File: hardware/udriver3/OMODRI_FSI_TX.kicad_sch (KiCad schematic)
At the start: 7 parts, among them J10 Conn_01x07, U13 TPD6E05U06, U14 DSLVDS1047

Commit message: Almost done, Rework power plane, change FSI DF13 (possibly wrong footprint (see pin 1), add 3d for all components, connect VM and 12V0, ...
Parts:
- J10: footprint udriver3:Hirose_DF13-07P-1.25DSA_1x07_P1.25mm_Vertical -> udriver3:DF137P125H75
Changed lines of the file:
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@@
       (effects (font (size 1.27 1.27)) (justify left))
     )
-    (property "Footprint" "udriver3:Hirose_DF13-07P-1.25DSA_1x07_P1.25mm_Vertical" (id 2) (at 241.935 80.645 0)
+    (property "Footprint" "udriver3:DF137P125H75" (id 2) (at 241.935 80.645 0)
       (effects (font (size 1.27 1.27)) hide)
     )

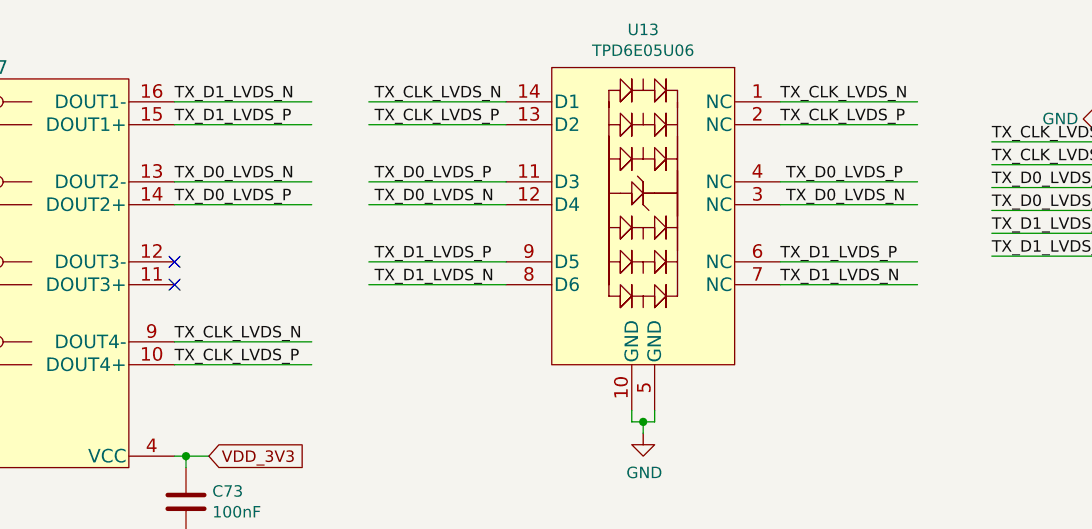
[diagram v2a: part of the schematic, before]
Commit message: Schematics update. 12V0 and 5V0 power supplies not finished yet. RS485 added but not connected to F28388 mcu.
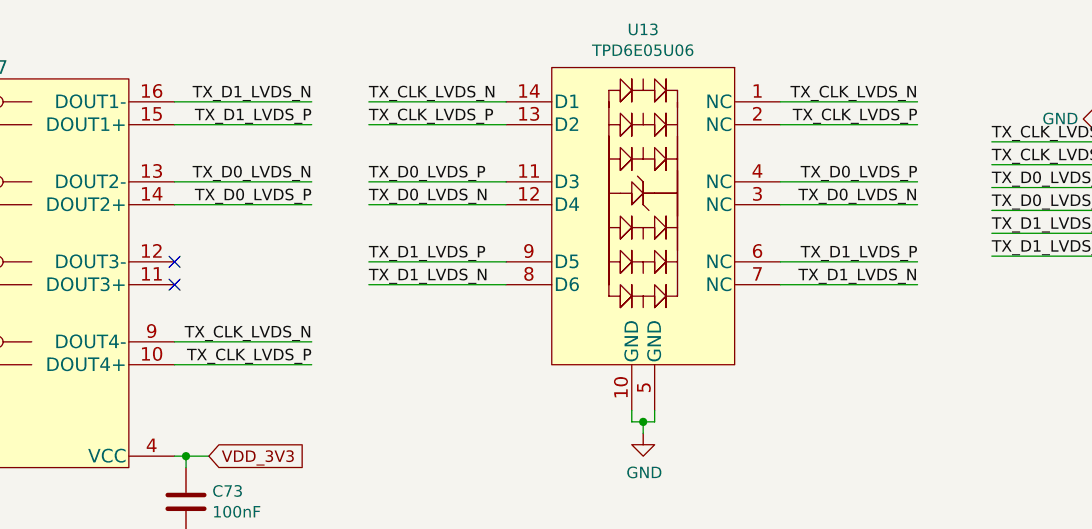
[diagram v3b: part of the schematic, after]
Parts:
- C73: Rated Voltage 10V -> 25V
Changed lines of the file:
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@@
     (title "Open MOtor DRiver Initiative (OMODRI)")
     (date "2020-12-16")
-    (rev "1.1")
+    (rev "2.0")
     (company "LAAS/CNRS")
   )
@@
     (stroke (width 0) (type default) (color 0 0 0 0))
   )
-  (label "TX_D0_LVDS_P" (at 153.035 80.01 0)
+  (label "TX_D0_LVDS_P" (at 152.4 80.01 0)
     (effects (font (size 1.27 1.27)) (justify left bottom))
   )
@@
     (effects (font (size 1.27 1.27)) (justify left bottom))
   )
-  (label "TX_CLK_LVDS_N" (at 153.035 71.12 0)
-    (effects (font (size 1.27 1.27)) (justify left bottom))
-  )
-  (label "TX_D0_LVDS_N" (at 198.755 82.55 0)
-    (effects (font (size 1.27 1.27)) (justify left bottom))
-  )
-  (label "TX_CLK_LVDS_P" (at 153.035 73.66 0)
-    (effects (font (size 1.27 1.27)) (justify left bottom))
-  )
-  (label "TX_CLK_LVDS_P" (at 198.12 73.66 0)
-    (effects (font (size 1.27 1.27)) (justify left bottom))
-  )
-  (label "TX_D1_LVDS_P" (at 130.81 73.66 0)
-    (effects (font (size 1.27 1.27)) (justify left bottom))
-  )
-  (label "TX_D1_LVDS_N" (at 130.81 71.12 0)
-    (effects (font (size 1.27 1.27)) (justify left bottom))
-  )
-  (label "TX_D0_LVDS_N" (at 153.035 82.55 0)
-    (effects (font (size 1.27 1.27)) (justify left bottom))
-  )
-  (label "TX_D0_LVDS_P" (at 198.755 80.01 0)
-    (effects (font (size 1.27 1.27)) (justify left bottom))
+  (label "TX_CLK_LVDS_N" (at 152.4 71.12 0)
+    (effects (font (size 1.27 1.27)) (justify left bottom))
+  )
+  (label "TX_D0_LVDS_N" (at 213.36 82.55 180)
+    (effects (font (size 1.27 1.27)) (justify right bottom))
+  )
+  (label "TX_CLK_LVDS_P" (at 152.4 73.66 0)
+    (effects (font (size 1.27 1.27)) (justify left bottom))
+  )
+  (label "TX_CLK_LVDS_P" (at 213.36 73.66 180)
+    (effects (font (size 1.27 1.27)) (justify right bottom))
+  )
+  (label "TX_D1_LVDS_P" (at 146.05 73.66 180)
+    (effects (font (size 1.27 1.27)) (justify right bottom))
+  )
+  (label "TX_D1_LVDS_N" (at 146.05 71.12 180)
+    (effects (font (size 1.27 1.27)) (justify right bottom))
+  )
+  (label "TX_D0_LVDS_N" (at 152.4 82.55 0)
+    (effects (font (size 1.27 1.27)) (justify left bottom))
+  )
+  (label "TX_D0_LVDS_P" (at 213.36 80.01 180)
+    (effects (font (size 1.27 1.27)) (justify right bottom))
   )
   (label "TX_D1_LVDS_N" (at 221.615 88.265 0)
     (effects (font (size 1.27 1.27)) (justify left bottom))
   )
-  (label "TX_D0_LVDS_P" (at 130.81 82.55 0)
-    (effects (font (size 1.27 1.27)) (justify left bottom))
+  (label "TX_D0_LVDS_P" (at 146.05 82.55 180)
+    (effects (font (size 1.27 1.27)) (justify right bottom))
   )
   (label "TX_CLK_LVDS_N" (at 221.615 75.565 0)
     (effects (font (size 1.27 1.27)) (justify left bottom))
   )
-  (label "TX_D1_LVDS_N" (at 153.035 91.44 0)
-    (effects (font (size 1.27 1.27)) (justify left bottom))
-  )
-  (label "TX_D1_LVDS_N" (at 198.12 91.44 0)
-    (effects (font (size 1.27 1.27)) (justify left bottom))
-  )
-  (label "TX_D0_LVDS_N" (at 130.81 80.01 0)
-    (effects (font (size 1.27 1.27)) (justify left bottom))
+  (label "TX_D1_LVDS_N" (at 152.4 91.44 0)
+    (effects (font (size 1.27 1.27)) (justify left bottom))
+  )
+  (label "TX_D1_LVDS_N" (at 213.36 91.44 180)
+    (effects (font (size 1.27 1.27)) (justify right bottom))
+  )
+  (label "TX_D0_LVDS_N" (at 146.05 80.01 180)
+    (effects (font (size 1.27 1.27)) (justify right bottom))
   )
   (label "TX_D0_LVDS_N" (at 221.615 80.645 0)
     (effects (font (size 1.27 1.27)) (justify left bottom))
   )
-  (label "TX_D1_LVDS_P" (at 153.035 88.9 0)
-    (effects (font (size 1.27 1.27)) (justify left bottom))
-  )
-  (label "TX_CLK_LVDS_P" (at 130.81 100.33 0)
-    (effects (font (size 1.27 1.27)) (justify left bottom))
+  (label "TX_D1_LVDS_P" (at 152.4 88.9 0)
+    (effects (font (size 1.27 1.27)) (justify left bottom))
+  )
+  (label "TX_CLK_LVDS_P" (at 146.05 100.33 180)
+    (effects (font (size 1.27 1.27)) (justify right bottom))
   )
   (label "TX_D1_LVDS_P" (at 221.615 85.725 0)
     (effects (font (size 1.27 1.27)) (justify left bottom))
   )
-  (label "TX_CLK_LVDS_N" (at 198.12 71.12 0)
-    (effects (font (size 1.27 1.27)) (justify left bottom))
-  )
-  (label "TX_CLK_LVDS_N" (at 130.81 97.79 0)
-    (effects (font (size 1.27 1.27)) (justify left bottom))
-  )
-  (label "TX_D1_LVDS_P" (at 198.12 88.9 0)
-    (effects (font (size 1.27 1.27)) (justify left bottom))
+  (label "TX_CLK_LVDS_N" (at 213.36 71.12 180)
+    (effects (font (size 1.27 1.27)) (justify right bottom))
+  )
+  (label "TX_CLK_LVDS_N" (at 146.05 97.79 180)
+    (effects (font (size 1.27 1.27)) (justify right bottom))
+  )
+  (label "TX_D1_LVDS_P" (at 213.36 88.9 180)
+    (effects (font (size 1.27 1.27)) (justify right bottom))
   )
   (global_label "VDD_3V3" (shape input) (at 134.62 110.49 0) (fields_autoplaced)
@@
       (effects (font (size 1.27 1.27)) hide)
     )
-    (property "Rated Voltage" "10V" (id 5) (at 132.08 115.57 0)
-      (effects (font (size 1.27 1.27)) hide)
-    )
+    (property "Rated Voltage" "25V" (id 5) (at 132.08 115.57 0)
+      (effects (font (size 1.27 1.27)) hide)
+    )

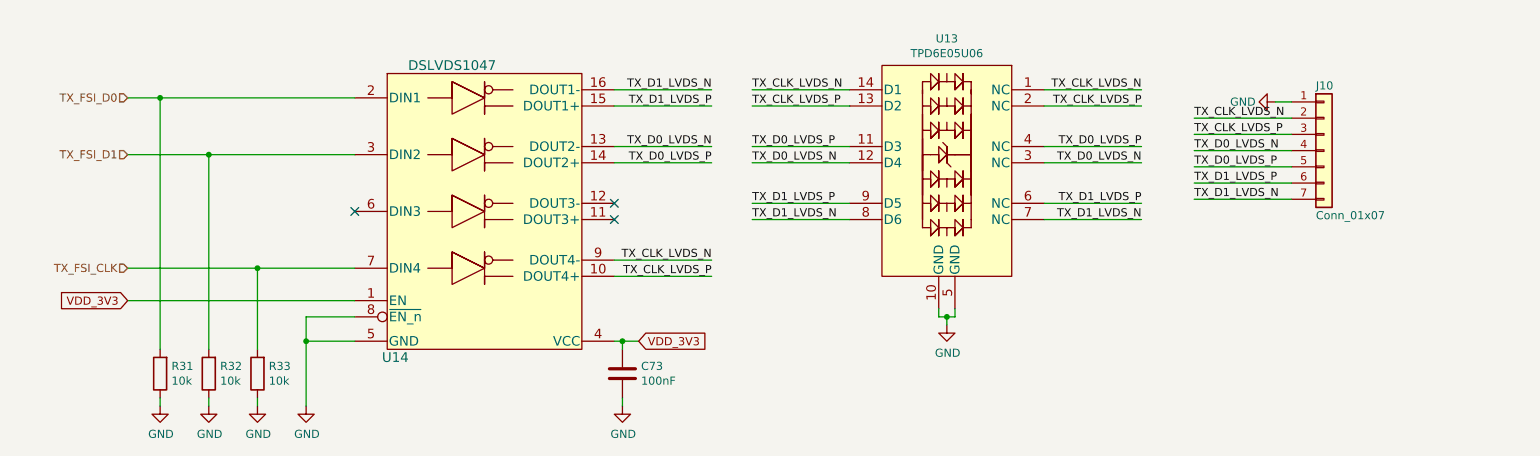
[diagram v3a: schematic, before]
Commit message: Temporary version of udrive3 v2.0. - In schematic there are 2 solutions for DC/DC buck converter. - PCB routing is not finished yet.
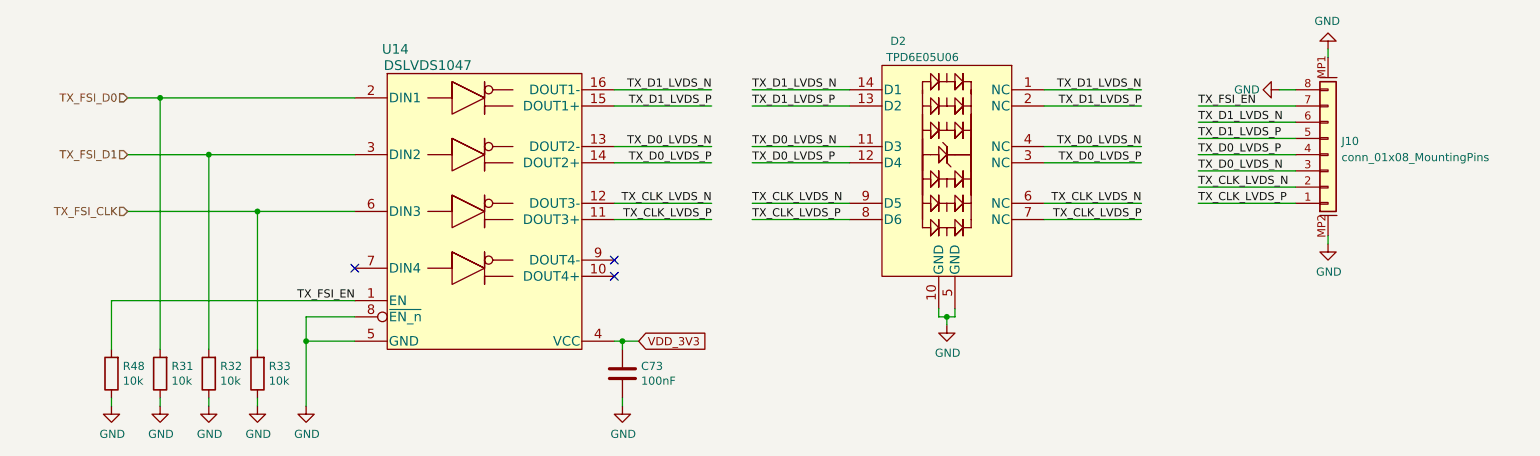
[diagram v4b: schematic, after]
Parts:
- removed J10: Conn_01x07, udriver3:DF137P125H75, symbol Connector_Generic:Conn_01x07
- added J10: conn_01x08_MountingPins, udriver3:Molex_FBH1_1x08-2MP_P0.50mm_Horizontal, symbol omodri_lib:conn_01x08_MountingPins
- added R48: 10k, Resistor_SMD:R_0201_0603Metric, symbol Device:R
- D2: renamed from U13; footprint udriver3:USON_14 -> udrive3:USON_14
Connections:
- net GND: now also J10.8 (Pin_8), J10.MP1 (MountPin1), J10.MP2 (MountPin2), R48.1
- net TX_CLK_LVDS_N: now also D2.6 (NC), D2.9 (D5), U14.12 (DOUT3-), J10.2 (Pin_2); no longer D2.1 (NC), D2.14 (D1), U14.9 (DOUT4-)
- net TX_CLK_LVDS_P: now also D2.7 (NC), D2.8 (D6), U14.11 (DOUT3+), J10.1 (Pin_1); no longer D2.13 (D2), D2.2 (NC), U14.10 (DOUT4+)
- net TX_D0_LVDS_N: now also D2.11 (D3), D2.4 (NC), J10.3 (Pin_3); no longer D2.12 (D4), D2.3 (NC)
- net TX_D0_LVDS_P: now also D2.12 (D4), D2.3 (NC), J10.4 (Pin_4); no longer D2.11 (D3), D2.4 (NC)
- net TX_D1_LVDS_N: now also D2.1 (NC), D2.14 (D1), J10.6 (Pin_6); no longer D2.7 (NC), D2.8 (D6)
- net TX_D1_LVDS_P: now also D2.13 (D2), D2.2 (NC), J10.5 (Pin_5); no longer D2.6 (NC), D2.9 (D5)
- net TX_FSI_CLK: now also U14.6 (DIN3); no longer U14.7 (DIN4)
- net VDD_3V3: no longer U14.1 (EN)
- new net TX_FSI_EN: J10.7 (Pin_7), R48.2, U14.1 (EN)

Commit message: Some routing updates.
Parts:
- D2: footprint udrive3:USON_14 -> udriver3:USON_14
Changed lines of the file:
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@@
     (property "Reference" "D2" (id 0) (at 175.26 63.5 0))
     (property "Value" "TPD6E05U06" (id 1) (at 179.07 66.04 0))
-    (property "Footprint" "udrive3:USON_14" (id 2) (at 182.88 81.28 90)
+    (property "Footprint" "udriver3:USON_14" (id 2) (at 182.88 81.28 90)
       (effects (font (size 1.27 1.27)) hide)
     )

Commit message: PCB routing update.
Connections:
- net TX_FSI_CLK renamed FSI_TX_CLK
- net TX_FSI_D0 renamed FSI_TX_D0
- net TX_FSI_D1 renamed FSI_TX_D1
- net TX_FSI_EN renamed FSI_TX_EN
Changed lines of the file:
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@@
     (effects (font (size 1.27 1.27)) (justify left bottom))
   )
-  (label "TX_FSI_EN" (at 222.25 73.66 0)
+  (label "FSI_TX_EN" (at 222.25 73.66 0)
     (effects (font (size 1.27 1.27)) (justify left bottom))
   )
@@
     (effects (font (size 1.27 1.27)) (justify right bottom))
   )
-  (label "TX_FSI_EN" (at 90.17 104.14 180)
+  (label "FSI_TX_EN" (at 90.17 104.14 180)
     (effects (font (size 1.27 1.27)) (justify right bottom))
   )
@@
     )
   )
-  (hierarchical_label "TX_FSI_D0" (shape input) (at 54.61 72.39 180)
+  (hierarchical_label "FSI_TX_D0" (shape input) (at 54.61 72.39 180)
     (effects (font (size 1.27 1.27)) (justify right))
   )
-  (hierarchical_label "TX_FSI_CLK" (shape input) (at 54.61 90.17 180)
+  (hierarchical_label "FSI_TX_CLK" (shape input) (at 54.61 90.17 180)
     (effects (font (size 1.27 1.27)) (justify right))
   )
-  (hierarchical_label "TX_FSI_D1" (shape input) (at 54.61 81.28 180)
+  (hierarchical_label "FSI_TX_D1" (shape input) (at 54.61 81.28 180)
     (effects (font (size 1.27 1.27)) (justify right))
   )

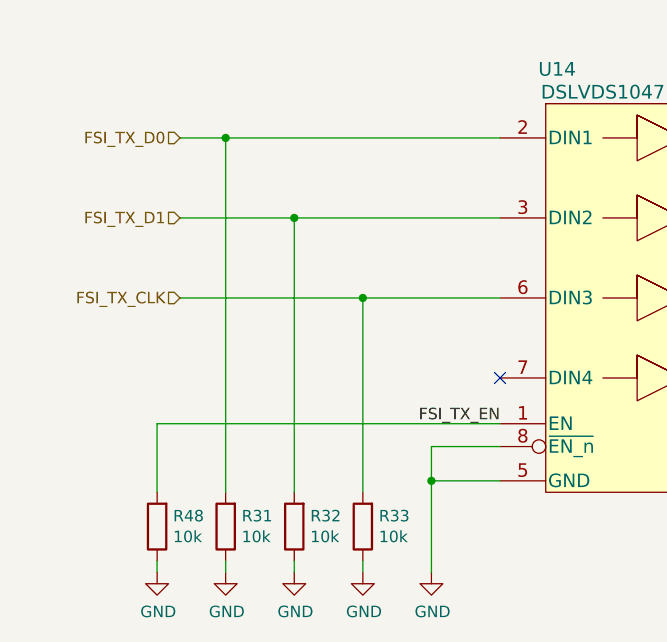
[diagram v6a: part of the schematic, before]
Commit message: Power supplies updates. Previous 12V & 5V need to be removed.
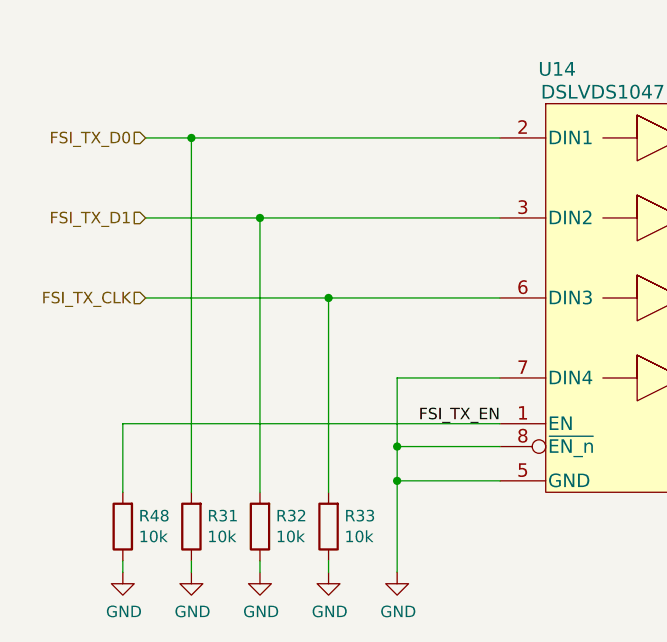
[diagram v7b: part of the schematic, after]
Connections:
- net GND: now also U14.7 (DIN4)
- no-connect marks 3 -> 2
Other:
- moved on the sheet: R31, R32, R33, R48

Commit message: PCB update. Re-annotation of the design + via stitching (GND).
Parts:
- renumbered C73 to C14, D2 to D3, J10 to J7, R48 to R15, R31 to R16, R32 to R17, R33 to R18, U14 to U5
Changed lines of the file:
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@@
   (symbol (lib_id "power:GND") (at 132.08 120.65 0) (unit 1)
     (in_bom yes) (on_board yes)
-    (property "Reference" "#PWR093" (id 0) (at 132.08 127 0)
+    (property "Reference" "#PWR057" (id 0) (at 132.08 127 0)
       (effects (font (size 1.27 1.27)) hide)
     )
@@
   (symbol (lib_id "Device:C") (at 132.08 115.57 0) (unit 1)
     (in_bom yes) (on_board yes)
-    (property "Reference" "C73" (id 0) (at 135.001 114.4016 0)
+    (property "Reference" "C14" (id 0) (at 135.001 114.4016 0)
       (effects (font (size 1.27 1.27)) (justify left))
     )
@@
   (symbol (lib_id "power:GND") (at 78.74 120.65 0) (unit 1)
     (in_bom yes) (on_board yes)
-    (property "Reference" "#PWR092" (id 0) (at 78.74 127 0)
+    (property "Reference" "#PWR056" (id 0) (at 78.74 127 0)
       (effects (font (size 1.27 1.27)) hide)
     )
@@
   (symbol (lib_id "Device:R") (at 55.88 115.57 180) (unit 1)
     (in_bom yes) (on_board yes)
-    (property "Reference" "R31" (id 0) (at 57.658 114.4016 0)
+    (property "Reference" "R16" (id 0) (at 57.658 114.4016 0)
       (effects (font (size 1.27 1.27)) (justify right))
     )
@@
   (symbol (lib_id "Device:R") (at 63.5 115.57 180) (unit 1)
     (in_bom yes) (on_board yes)
-    (property "Reference" "R32" (id 0) (at 65.278 114.4016 0)
+    (property "Reference" "R17" (id 0) (at 65.278 114.4016 0)
       (effects (font (size 1.27 1.27)) (justify right))
     )
@@
   (symbol (lib_id "Device:R") (at 71.12 115.57 180) (unit 1)
     (in_bom yes) (on_board yes)
-    (property "Reference" "R33" (id 0) (at 72.898 114.4016 0)
+    (property "Reference" "R18" (id 0) (at 72.898 114.4016 0)
       (effects (font (size 1.27 1.27)) (justify right))
     )
@@
   (symbol (lib_id "power:GND") (at 55.88 120.65 0) (unit 1)
     (in_bom yes) (on_board yes)
-    (property "Reference" "#PWR089" (id 0) (at 55.88 127 0)
+    (property "Reference" "#PWR053" (id 0) (at 55.88 127 0)
       (effects (font (size 1.27 1.27)) hide)
     )
@@
   (symbol (lib_id "power:GND") (at 63.5 120.65 0) (unit 1)
     (in_bom yes) (on_board yes)
-    (property "Reference" "#PWR090" (id 0) (at 63.5 127 0)
+    (property "Reference" "#PWR054" (id 0) (at 63.5 127 0)
       (effects (font (size 1.27 1.27)) hide)
     )
@@
   (symbol (lib_id "power:GND") (at 71.12 120.65 0) (unit 1)
     (in_bom yes) (on_board yes)
-    (property "Reference" "#PWR091" (id 0) (at 71.12 127 0)
+    (property "Reference" "#PWR055" (id 0) (at 71.12 127 0)
       (effects (font (size 1.27 1.27)) hide)
     )
@@
   (symbol (lib_id "omodri_lib:TPD6E05U06") (at 182.88 81.28 0) (unit 1)
     (in_bom yes) (on_board yes)
-    (property "Reference" "D2" (id 0) (at 175.26 63.5 0))
+    (property "Reference" "D3" (id 0) (at 175.26 63.5 0))
     (property "Value" "TPD6E05U06" (id 1) (at 179.07 66.04 0))
     (property "Footprint" "udriver3:USON_14" (id 2) (at 182.88 81.28 90)
@@
   (symbol (lib_id "power:GND") (at 182.88 107.95 0) (unit 1)
     (in_bom yes) (on_board yes)
-    (property "Reference" "#PWR088" (id 0) (at 182.88 114.3 0)
+    (property "Reference" "#PWR051" (id 0) (at 182.88 114.3 0)
       (effects (font (size 1.27 1.27)) hide)
     )
@@
   (symbol (lib_id "omodri_lib:DSLVDS1047PWR") (at 110.49 88.9 0) (unit 1)
     (in_bom yes) (on_board yes)
-    (property "Reference" "U14" (id 0) (at 96.52 64.77 0)
+    (property "Reference" "U5" (id 0) (at 96.52 64.77 0)
       (effects (font (size 1.524 1.524)))
     )
@@
   (symbol (lib_id "power:GND") (at 242.57 95.25 0) (unit 1)
     (in_bom yes) (on_board yes)
-    (property "Reference" "#PWR021" (id 0) (at 242.57 101.6 0)
+    (property "Reference" "#PWR050" (id 0) (at 242.57 101.6 0)
       (effects (font (size 1.27 1.27)) hide)
     )
@@
   (symbol (lib_id "power:GND") (at 234.95 71.12 270) (unit 1)
     (in_bom yes) (on_board yes)
-    (property "Reference" "#PWR020" (id 0) (at 228.6 71.12 0)
+    (property "Reference" "#PWR049" (id 0) (at 228.6 71.12 0)
       (effects (font (size 1.27 1.27)) hide)
     )
@@
   )
   (symbol (lib_id "omodri_lib:conn_01x08_MountingPins") (at 242.57 80.01 0) (mirror x) (unit 1)
-    (in_bom yes) (on_board yes) (fields_autoplaced)
-    (property "Reference" "J10" (id 0) (at 244.6782 79.1753 0)
+    (in_bom yes) (on_board yes)
+    (property "Reference" "J7" (id 0) (at 237.49 91.44 0)
       (effects (font (size 1.27 1.27)) (justify left))
     )
-    (property "Value" "conn_01x08_MountingPins" (id 1) (at 244.6782 81.7122 0)
+    (property "Value" "conn_01x08_MountingPins" (id 1) (at 245.11 67.31 90)
       (effects (font (size 1.27 1.27)) (justify left))
     )
@@
   (symbol (lib_id "Device:R") (at 48.26 115.57 180) (unit 1)
     (in_bom yes) (on_board yes)
-    (property "Reference" "R48" (id 0) (at 50.038 114.4016 0)
+    (property "Reference" "R15" (id 0) (at 50.038 114.4016 0)
       (effects (font (size 1.27 1.27)) (justify right))
     )
@@
   (symbol (lib_id "power:GND") (at 48.26 120.65 0) (unit 1)
     (in_bom yes) (on_board yes)
-    (property "Reference" "#PWR038" (id 0) (at 48.26 127 0)
+    (property "Reference" "#PWR052" (id 0) (at 48.26 127 0)
       (effects (font (size 1.27 1.27)) hide)
     )
@@
   (symbol (lib_id "power:GND") (at 242.57 64.77 180) (unit 1)
     (in_bom yes) (on_board yes)
-    (property "Reference" "#PWR019" (id 0) (at 242.57 58.42 0)
-      (effects (font (size 1.27 1.27)) hide)
-    )
+    (property "Reference" "#PWR048" (id 0) (at 242.57 58.42 0)
+      (effects (font (size 1.27 1.27)) hide)
+    )
